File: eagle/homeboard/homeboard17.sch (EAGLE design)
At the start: 128 parts, among them IC1 XCF02S, IC2 25LC080SN, IC3 ATMEGA32U2-TQFP, Q5 BC848SMD, Q6 BC848SMD, Q7 BC848SMD, Q8 BC848SMD, T1 BSS138, T2 BC848, T3 BSS138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

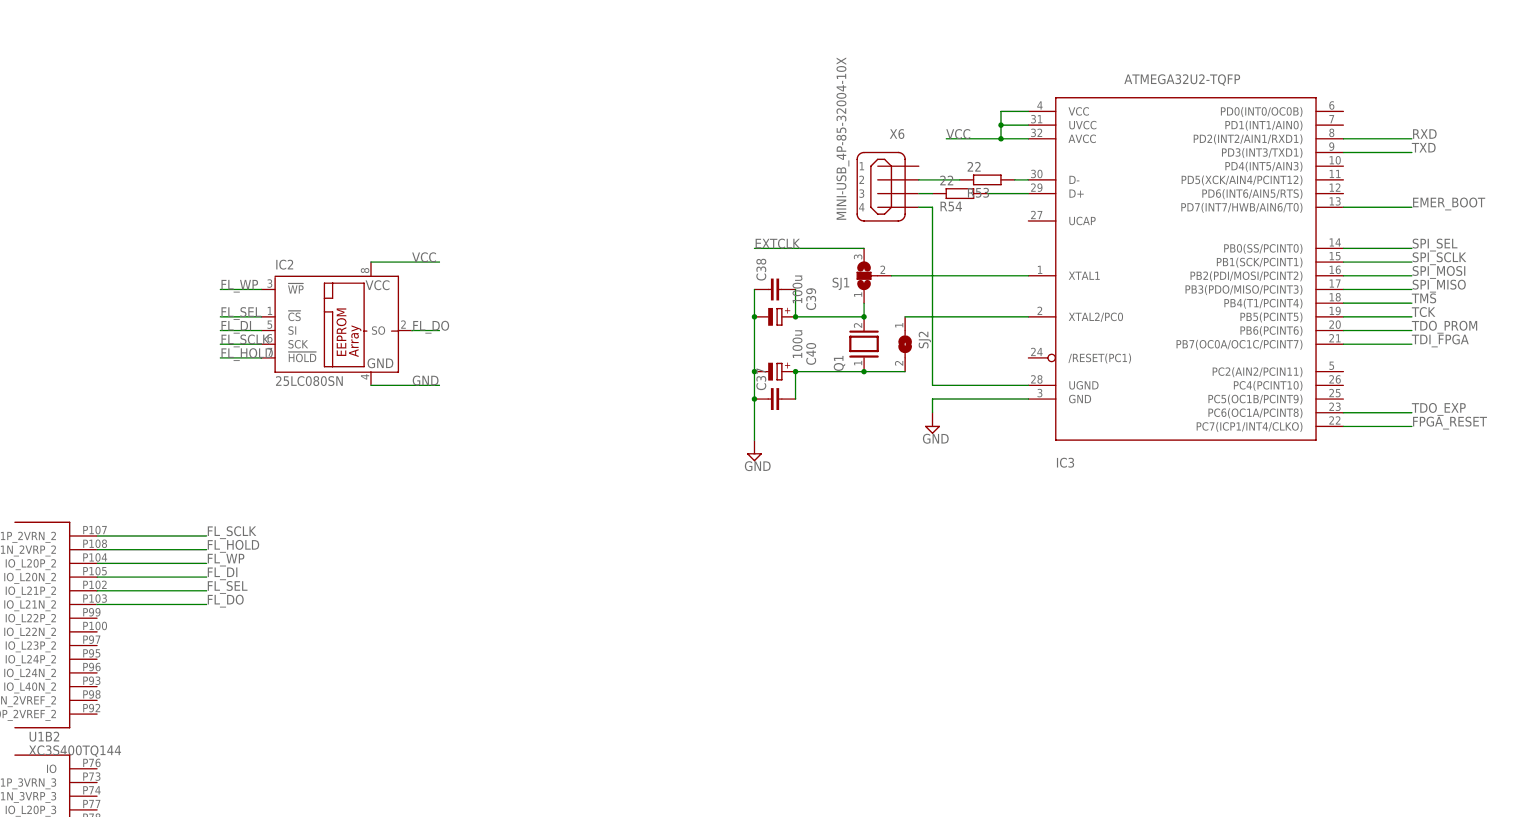
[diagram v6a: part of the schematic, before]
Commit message: added some more atmega pins
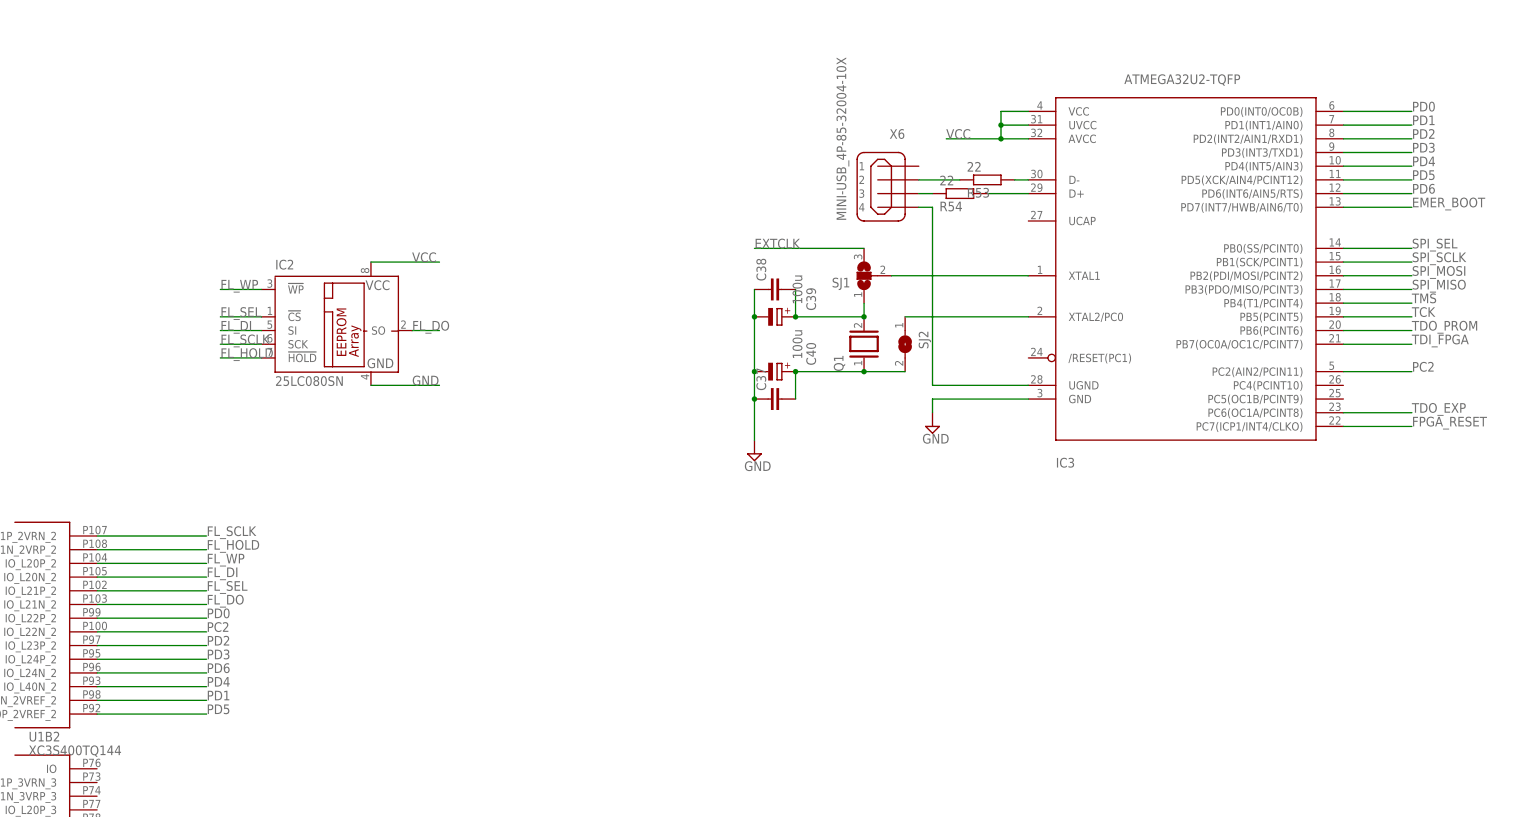
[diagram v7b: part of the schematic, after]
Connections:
- removed net RXD: IC3.PD2(INT2/AIN1/RXD1)
- removed net TXD: IC3.PD3(INT3/TXD1)
- new net PC2: IC3.PC2(AIN2/PCIN11), U1B2.IO_L22N_2
- new net PD0: IC3.PD0(INT0/OC0B), U1B2.IO_L22P_2
- new net PD1: IC3.PD1(INT1/AIN0), U1B2.IO_L23N_2VREF_2
- new net PD2: IC3.PD2(INT2/AIN1/RXD1), U1B2.IO_L23P_2
- new net PD3: IC3.PD3(INT3/TXD1), U1B2.IO_L24P_2
- new net PD4: IC3.PD4(INT5/AIN3), U1B2.IO_L40N_2
- new net PD5: IC3.PD5(XCK/AIN4/PCINT12), U1B2.IO_L40P_2VREF_2
- new net PD6: IC3.PD6(INT6/AIN5/RTS), U1B2.IO_L24N_2
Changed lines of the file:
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@@
 </segment>
 </net>
-<net name="RXD" class="0">
+<net name="PD2" class="0">
 <segment>
 <pinref part="IC3" gate="G$1" pin="PD2(INT2/AIN1/RXD1)"/>
@@
 <label x="454.66" y="129.54" size="1.778" layer="95"/>
 </segment>
-</net>
-<net name="TXD" class="0">
+<segment>
+<pinref part="U1" gate="B2" pin="IO_L23P_2"/>
+<wire x1="231.14" y1="35.56" x2="210.82" y2="35.56" width="0.1524" layer="91"/>
+<label x="231.14" y="35.56" size="1.778" layer="95"/>
+</segment>
+</net>
+<net name="PD3" class="0">
 <segment>
 <pinref part="IC3" gate="G$1" pin="PD3(INT3/TXD1)"/>
 <wire x1="454.66" y1="127" x2="441.96" y2="127" width="0.1524" layer="91"/>
 <label x="454.66" y="127" size="1.778" layer="95"/>
+</segment>
+<segment>
+<pinref part="U1" gate="B2" pin="IO_L24P_2"/>
+<wire x1="231.14" y1="33.02" x2="210.82" y2="33.02" width="0.1524" layer="91"/>
+<label x="231.14" y="33.02" size="1.778" layer="95"/>
 </segment>
 </net>
@@
 </segment>
 </net>
+<net name="PC2" class="0">
+<segment>
+<pinref part="IC3" gate="G$1" pin="PC2(AIN2/PCIN11)"/>
+<wire x1="454.66" y1="86.36" x2="441.96" y2="86.36" width="0.1524" layer="91"/>
+<label x="454.66" y="86.36" size="1.778" layer="95"/>
+</segment>
+<segment>
+<pinref part="U1" gate="B2" pin="IO_L22N_2"/>
+<wire x1="231.14" y1="38.1" x2="210.82" y2="38.1" width="0.1524" layer="91"/>
+<label x="231.14" y="38.1" size="1.778" layer="95"/>
+</segment>
+</net>
+<net name="PD0" class="0">
+<segment>
+<pinref part="IC3" gate="G$1" pin="PD0(INT0/OC0B)"/>
+<wire x1="454.66" y1="134.62" x2="441.96" y2="134.62" width="0.1524" layer="91"/>
+<label x="454.66" y="134.62" size="1.778" layer="95"/>
+</segment>
+<segment>
+<pinref part="U1" gate="B2" pin="IO_L22P_2"/>
+<wire x1="231.14" y1="40.64" x2="210.82" y2="40.64" width="0.1524" layer="91"/>
+<label x="231.14" y="40.64" size="1.778" layer="95"/>
+</segment>
+</net>
+<net name="PD1" class="0">
+<segment>
+<pinref part="IC3" gate="G$1" pin="PD1(INT1/AIN0)"/>
+<wire x1="454.66" y1="132.08" x2="441.96" y2="132.08" width="0.1524" layer="91"/>
+<label x="454.66" y="132.08" size="1.778" layer="95"/>
+</segment>
+<segment>
+<pinref part="U1" gate="B2" pin="IO_L23N_2VREF_2"/>
+<wire x1="231.14" y1="25.4" x2="210.82" y2="25.4" width="0.1524" layer="91"/>
+<label x="231.14" y="25.4" size="1.778" layer="95"/>
+</segment>
+</net>
+<net name="PD4" class="0">
+<segment>
+<pinref part="IC3" gate="G$1" pin="PD4(INT5/AIN3)"/>
+<wire x1="454.66" y1="124.46" x2="441.96" y2="124.46" width="0.1524" layer="91"/>
+<label x="454.66" y="124.46" size="1.778" layer="95"/>
+</segment>
+<segment>
+<pinref part="U1" gate="B2" pin="IO_L40N_2"/>
+<wire x1="231.14" y1="27.94" x2="210.82" y2="27.94" width="0.1524" layer="91"/>
+<label x="231.14" y="27.94" size="1.778" layer="95"/>
+</segment>
+</net>
+<net name="PD5" class="0">
+<segment>
+<pinref part="IC3" gate="G$1" pin="PD5(XCK/AIN4/PCINT12)"/>
+<wire x1="454.66" y1="121.92" x2="441.96" y2="121.92" width="0.1524" layer="91"/>
+<label x="454.66" y="121.92" size="1.778" layer="95"/>
+</segment>
+<segment>
+<pinref part="U1" gate="B2" pin="IO_L40P_2VREF_2"/>
+<wire x1="231.14" y1="22.86" x2="210.82" y2="22.86" width="0.1524" layer="91"/>
+<label x="231.14" y="22.86" size="1.778" layer="95"/>
+</segment>
+</net>
+<net name="PD6" class="0">
+<segment>
+<pinref part="IC3" gate="G$1" pin="PD6(INT6/AIN5/RTS)"/>
+<wire x1="454.66" y1="119.38" x2="441.96" y2="119.38" width="0.1524" layer="91"/>
+<label x="454.66" y="119.38" size="1.778" layer="95"/>
+</segment>
+<segment>
+<pinref part="U1" gate="B2" pin="IO_L24N_2"/>
+<wire x1="231.14" y1="30.48" x2="210.82" y2="30.48" width="0.1524" layer="91"/>
+<label x="231.14" y="30.48" size="1.778" layer="95"/>
+</segment>
+</net>

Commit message: mah
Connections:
- removed net N$10: IC3.XTAL2/PC0, SJ2.1
- removed net N$9: IC3.XTAL1, SJ1.2
- net N$12: now also IC3.XTAL2/PC0; no longer SJ2.2
- net N$14: now also IC3.XTAL1; no longer SJ1.1
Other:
- moved on the sheet: C37, C38, C39, C40, Q1, SJ1, SJ2
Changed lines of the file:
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@@
 <instance part="SV1" gate="1" x="43.18" y="-58.42" rot="R270"/>
 <instance part="SUPPLY19" gate="GND" x="109.22" y="83.82"/>
-<instance part="Q1" gate="G$1" x="353.06" y="91.44" rot="R90"/>
-<instance part="SJ1" gate="G$1" x="353.06" y="104.14" rot="R180"/>
-<instance part="SJ2" gate="1" x="360.68" y="91.44" rot="R270"/>
-<instance part="C37" gate="G$1" x="335.28" y="81.28" rot="R90"/>
-<instance part="C38" gate="G$1" x="335.28" y="101.6" rot="R90"/>
-<instance part="SUPPLY20" gate="GND" x="332.74" y="71.12"/>
-<instance part="C39" gate="G$1" x="337.82" y="96.52" smashed="yes" rot="R270">
+<instance part="Q1" gate="G$1" x="353.06" y="101.6" rot="R90"/>
+<instance part="SJ1" gate="G$1" x="378.46" y="50.8" rot="R180"/>
+<instance part="SJ2" gate="1" x="386.08" y="38.1" rot="R270"/>
+<instance part="C37" gate="G$1" x="335.28" y="91.44" rot="R90"/>
+<instance part="C38" gate="G$1" x="335.28" y="111.76" rot="R90"/>
+<instance part="SUPPLY20" gate="GND" x="332.74" y="81.28"/>
+<instance part="C39" gate="G$1" x="337.82" y="106.68" smashed="yes" rot="R270">
+<attribute name="NAME" x="342.3666" y="112.141" size="1.778" layer="95" rot="R270"/>
+<attribute name="VALUE" x="339.8266" y="114.554" size="1.778" layer="96" rot="R270"/>
+</instance>
+<instance part="C40" gate="G$1" x="337.82" y="96.52" smashed="yes" rot="R270">
 <attribute name="NAME" x="342.3666" y="101.981" size="1.778" layer="95" rot="R270"/>
 <attribute name="VALUE" x="339.8266" y="104.394" size="1.778" layer="96" rot="R270"/>
-</instance>
-<instance part="C40" gate="G$1" x="337.82" y="86.36" smashed="yes" rot="R270">
-<attribute name="NAME" x="342.3666" y="91.821" size="1.778" layer="95" rot="R270"/>
-<attribute name="VALUE" x="339.8266" y="94.234" size="1.778" layer="96" rot="R270"/>
 </instance>
 <instance part="PWR_HDR" gate="A" x="-297.18" y="50.8" rot="R90"/>
@@
 <pinref part="C38" gate="G$1" pin="1"/>
 <pinref part="C39" gate="G$1" pin="-"/>
-<wire x1="332.74" y1="101.6" x2="332.74" y2="96.52" width="0.1524" layer="91"/>
+<wire x1="332.74" y1="111.76" x2="332.74" y2="106.68" width="0.1524" layer="91"/>
 <pinref part="C40" gate="G$1" pin="-"/>
-<wire x1="332.74" y1="96.52" x2="332.74" y2="86.36" width="0.1524" layer="91"/>
+<wire x1="332.74" y1="106.68" x2="332.74" y2="96.52" width="0.1524" layer="91"/>
+<junction x="332.74" y="106.68"/>
+<pinref part="C37" gate="G$1" pin="1"/>
+<wire x1="332.74" y1="96.52" x2="332.74" y2="91.44" width="0.1524" layer="91"/>
 <junction x="332.74" y="96.52"/>
-<pinref part="C37" gate="G$1" pin="1"/>
-<wire x1="332.74" y1="86.36" x2="332.74" y2="81.28" width="0.1524" layer="91"/>
-<junction x="332.74" y="86.36"/>
 <pinref part="SUPPLY20" gate="GND" pin="GND"/>
-<wire x1="332.74" y1="73.66" x2="332.74" y2="81.28" width="0.1524" layer="91"/>
-<junction x="332.74" y="81.28"/>
+<wire x1="332.74" y1="83.82" x2="332.74" y2="91.44" width="0.1524" layer="91"/>
+<junction x="332.74" y="91.44"/>
 </segment>
 <segment>
@@
 </segment>
 </net>
-<net name="N$9" class="0">
-<segment>
-<pinref part="IC3" gate="G$1" pin="XTAL1"/>
-<pinref part="SJ1" gate="G$1" pin="2"/>
-<wire x1="383.54" y1="104.14" x2="358.14" y2="104.14" width="0.1524" layer="91"/>
-</segment>
-</net>
-<net name="N$10" class="0">
-<segment>
-<pinref part="IC3" gate="G$1" pin="XTAL2/PC0"/>
-<pinref part="SJ2" gate="1" pin="1"/>
-<wire x1="383.54" y1="96.52" x2="360.68" y2="96.52" width="0.1524" layer="91"/>
-</segment>
-</net>
 <net name="EXTCLK" class="0">
 <segment>
 <pinref part="SJ1" gate="G$1" pin="3"/>
-<wire x1="353.06" y1="109.22" x2="332.74" y2="109.22" width="0.1524" layer="91"/>
-<label x="332.74" y="109.22" size="1.778" layer="95"/>
+<wire x1="378.46" y1="55.88" x2="358.14" y2="55.88" width="0.1524" layer="91"/>
+<label x="358.14" y="55.88" size="1.778" layer="95"/>
 </segment>
 </net>
@@
 <pinref part="C37" gate="G$1" pin="2"/>
 <pinref part="C40" gate="G$1" pin="+"/>
-<wire x1="340.36" y1="81.28" x2="340.36" y2="86.36" width="0.1524" layer="91"/>
-<pinref part="SJ2" gate="1" pin="2"/>
+<wire x1="340.36" y1="91.44" x2="340.36" y2="96.52" width="0.1524" layer="91"/>
 <pinref part="Q1" gate="G$1" pin="1"/>
-<wire x1="360.68" y1="86.36" x2="353.06" y2="86.36" width="0.1524" layer="91"/>
-<wire x1="340.36" y1="86.36" x2="353.06" y2="86.36" width="0.1524" layer="91"/>
-<junction x="340.36" y="86.36"/>
-<junction x="353.06" y="86.36"/>
+<wire x1="340.36" y1="96.52" x2="353.06" y2="96.52" width="0.1524" layer="91"/>
+<junction x="340.36" y="96.52"/>
+<pinref part="IC3" gate="G$1" pin="XTAL2/PC0"/>
+<wire x1="383.54" y1="96.52" x2="353.06" y2="96.52" width="0.1524" layer="91"/>
+<junction x="353.06" y="96.52"/>
 </segment>
 </net>
@@
 <pinref part="C38" gate="G$1" pin="2"/>
 <pinref part="C39" gate="G$1" pin="+"/>
-<pinref part="SJ1" gate="G$1" pin="1"/>
 <pinref part="Q1" gate="G$1" pin="2"/>
-<wire x1="353.06" y1="96.52" x2="353.06" y2="99.06" width="0.1524" layer="91"/>
-<junction x="353.06" y="96.52"/>
-<wire x1="353.06" y1="96.52" x2="340.36" y2="96.52" width="0.1524" layer="91"/>
-<wire x1="340.36" y1="96.52" x2="340.36" y2="101.6" width="0.1524" layer="91"/>
-<junction x="340.36" y="96.52"/>
-</segment>
-</net>
+<wire x1="353.06" y1="106.68" x2="340.36" y2="106.68" width="0.1524" layer="91"/>
+<wire x1="340.36" y1="106.68" x2="340.36" y2="111.76" width="0.1524" layer="91"/>
+<junction x="340.36" y="106.68"/>
+<pinref part="IC3" gate="G$1" pin="XTAL1"/>
+<wire x1="383.54" y1="104.14" x2="360.68" y2="104.14" width="0.1524" layer="91"/>
+<wire x1="360.68" y1="104.14" x2="360.68" y2="106.68" width="0.1524" layer="91"/>
+<wire x1="360.68" y1="106.68" x2="353.06" y2="106.68" width="0.1524" layer="91"/>
+<junction x="353.06" y="106.68"/>
+</segment>
+</net>
